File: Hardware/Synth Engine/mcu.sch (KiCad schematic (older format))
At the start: 32 parts, among them J10 USB_C_Receptacle, J3 SWD_programming, J7 Capsense_buttons, U6 CY8C4246AZI-L445, Y1 16MHz, Y2 32.768kHz

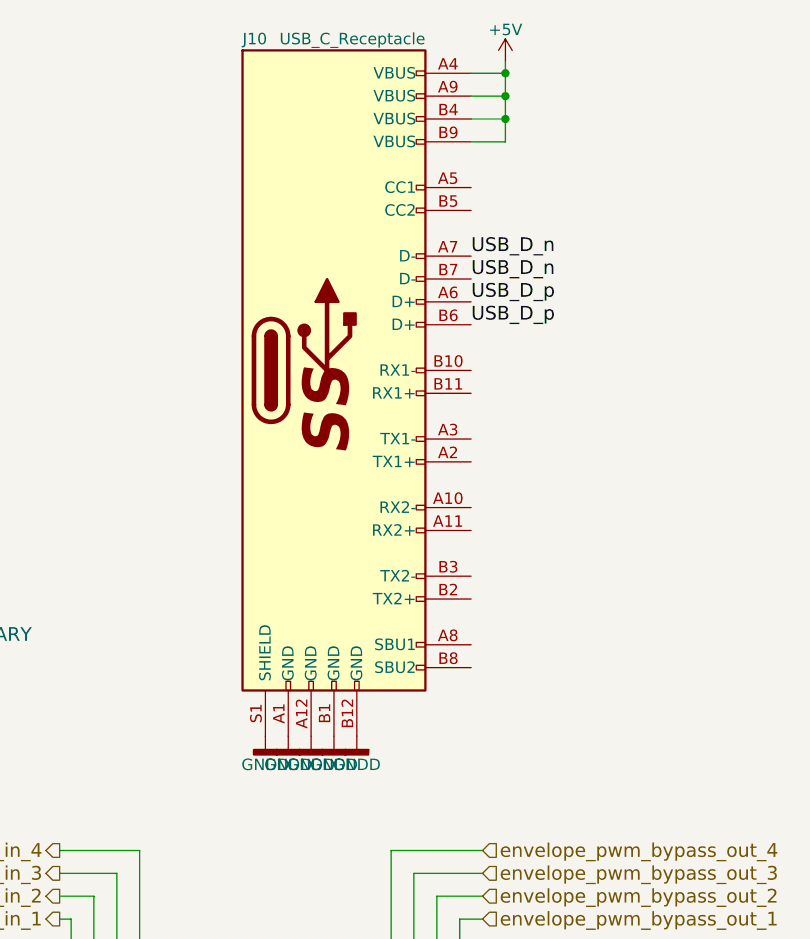
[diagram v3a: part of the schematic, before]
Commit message: redo second connector on main board
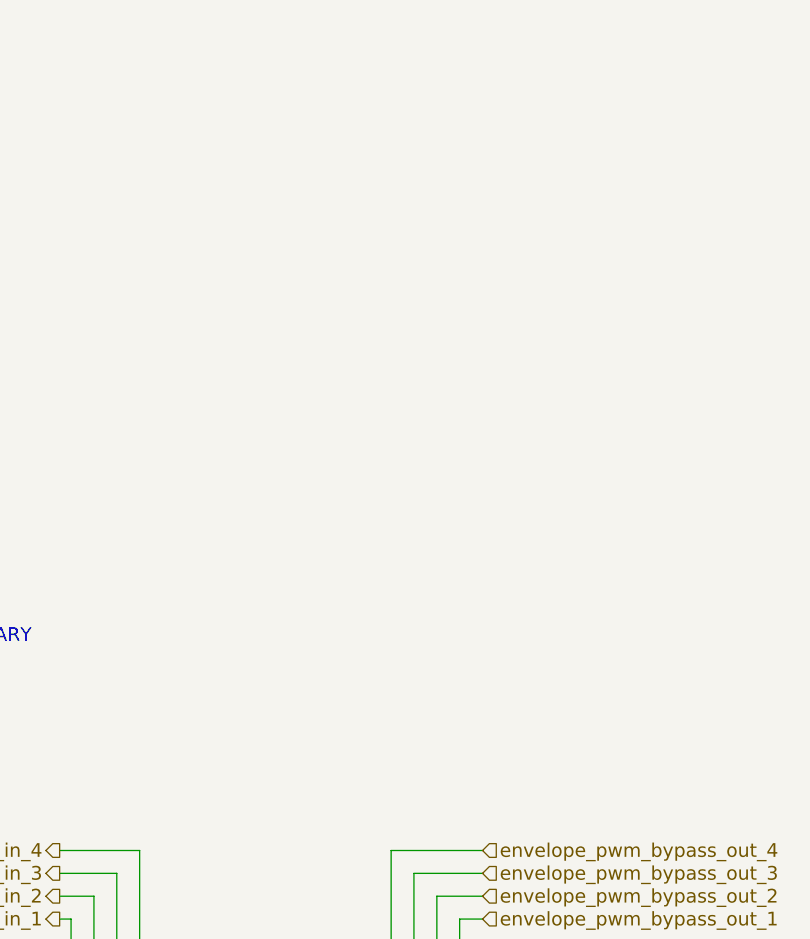
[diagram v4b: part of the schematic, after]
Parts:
- removed J10: USB_C_Receptacle, digikey-footprints:USB_Type_C_Female__12401610E4_2A, symbol USB_C_Receptacle
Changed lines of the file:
@@
 Text Notes 6350 3550 0    60   ~ 0
 Delay pins are TEMPORARY
-$Comp
-L USB_C_Receptacle J10
-U 1 1 5C748784
-P 8800 2350
-F 0 "J10" H 8400 3800 50  0000 L CNN
-F 1 "USB_C_Receptacle" H 9200 3800 50  0000 R CNN
-F 2 "digikey-footprints:USB_Type_C_Female__12401610E4_2A" H 8950 2350 50  0001 C CNN
-F 3 "" H 8950 2350 50  0001 C CNN
-	1    8800 2350
-	1    0    0    -1
-$EndComp
-$Comp
-L GNDD #PWR0106
-U 1 1 5C748857
-P 8900 3950
-F 0 "#PWR0106" H 8900 3700 50  0001 C CNN
-F 1 "GNDD" H 8900 3825 50  0000 C CNN
-F 2 "" H 8900 3950 50  0001 C CNN
-F 3 "" H 8900 3950 50  0001 C CNN
-	1    8900 3950
-	-1   0    0    -1
-$EndComp
-$Comp
-L GNDD #PWR0107
-U 1 1 5C74890A
-P 8800 3950
-F 0 "#PWR0107" H 8800 3700 50  0001 C CNN
-F 1 "GNDD" H 8800 3825 50  0000 C CNN
-F 2 "" H 8800 3950 50  0001 C CNN
-F 3 "" H 8800 3950 50  0001 C CNN
-	1    8800 3950
-	-1   0    0    -1
-$EndComp
-$Comp
-L GNDD #PWR0108
-U 1 1 5C748969
-P 8700 3950
-F 0 "#PWR0108" H 8700 3700 50  0001 C CNN
-F 1 "GNDD" H 8700 3825 50  0000 C CNN
-F 2 "" H 8700 3950 50  0001 C CNN
-F 3 "" H 8700 3950 50  0001 C CNN
-	1    8700 3950
-	-1   0    0    -1
-$EndComp
-$Comp
-L GNDD #PWR0109
-U 1 1 5C7489C8
-P 8600 3950
-F 0 "#PWR0109" H 8600 3700 50  0001 C CNN
-F 1 "GNDD" H 8600 3825 50  0000 C CNN
-F 2 "" H 8600 3950 50  0001 C CNN
-F 3 "" H 8600 3950 50  0001 C CNN
-	1    8600 3950
-	-1   0    0    -1
-$EndComp
-$Comp
-L GNDD #PWR0110
-U 1 1 5C748A27
-P 8500 3950
-F 0 "#PWR0110" H 8500 3700 50  0001 C CNN
-F 1 "GNDD" H 8500 3825 50  0000 C CNN
-F 2 "" H 8500 3950 50  0001 C CNN
-F 3 "" H 8500 3950 50  0001 C CNN
-	1    8500 3950
-	-1   0    0    -1
-$EndComp
-Text Label 9400 2150 0    60   ~ 0
-USB_D_p
-Text Label 9400 2050 0    60   ~ 0
-USB_D_p
-Text Label 9400 1950 0    60   ~ 0
-USB_D_n
-Text Label 9400 1850 0    60   ~ 0
-USB_D_n
 Text Label 2150 2850 2    60   ~ 0
 USB_D_p
@@
 USB_D_n
 $Comp
-L +5V #PWR0111
-U 1 1 5C74952F
-P 9550 1000
-F 0 "#PWR0111" H 9550 850 50  0001 C CNN
-F 1 "+5V" H 9550 1140 50  0000 C CNN
-F 2 "" H 9550 1000 50  0001 C CNN
-F 3 "" H 9550 1000 50  0001 C CNN
-	1    9550 1000
-	1    0    0    -1
-$EndComp
-$Comp
-L +5V #PWR0112
+L +5V #PWR0106
 U 1 1 5C7498B1
 P 2100 2600
-F 0 "#PWR0112" H 2100 2450 50  0001 C CNN
+F 0 "#PWR0106" H 2100 2450 50  0001 C CNN
 F 1 "+5V" H 2100 2740 50  0000 C CNN
 F 2 "" H 2100 2600 50  0001 C CNN
@@
 $EndComp
 $Comp
-L GNDD #PWR0113
+L GNDD #PWR0107
 U 1 1 5C74C9C5
 P 6050 2350
-F 0 "#PWR0113" H 6050 2100 50  0001 C CNN
+F 0 "#PWR0107" H 6050 2100 50  0001 C CNN
 F 1 "GNDD" H 6050 2225 50  0000 C CNN
 F 2 "" H 6050 2350 50  0001 C CNN
@@
 $EndComp
 $Comp
-L GNDD #PWR0114
+L GNDD #PWR0108
 U 1 1 5C74C9CB
 P 6550 2350
-F 0 "#PWR0114" H 6550 2100 50  0001 C CNN
+F 0 "#PWR0108" H 6550 2100 50  0001 C CNN
 F 1 "GNDD" H 6550 2225 50  0000 C CNN
 F 2 "" H 6550 2350 50  0001 C CNN
@@
 	5950 4500 5950 4450
 Wire Wire Line
-	9550 1000 9550 1350
-Wire Wire Line
-	9550 1350 9400 1350
-Wire Wire Line
-	9400 1250 9550 1250
-Connection ~ 9550 1250
-Wire Wire Line
-	9400 1150 9550 1150
-Connection ~ 9550 1150
-Wire Wire Line
-	9400 1050 9550 1050
-Connection ~ 9550 1050
-Wire Wire Line
 	2100 2600 2100 2650

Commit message: new release candidate. Passes DRC.
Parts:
- added J10: USB, Connectors_Molex:Molex_KK-6410-04_04x2.54mm_Straight, symbol Conn_01x04
- J7: footprint Pin_Headers:Pin_Header_Straight_1x04_Pitch2.54mm -> Connectors_Molex:Molex_KK-6410-04_04x2.54mm_Straight
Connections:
- net +5V: now also J10.1 (Pin_1)
- net GNDD: now also J10.4 (Pin_4)
- net USB_D_n: now also J10.2 (Pin_2)
- net USB_D_p: now also J10.3 (Pin_3)
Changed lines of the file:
@@
 F 0 "J7" H 6150 4550 50  0000 C CNN
 F 1 "Capsense_buttons" H 6550 4300 50  0000 C CNN
-F 2 "Pin_Headers:Pin_Header_Straight_1x04_Pitch2.54mm" H 6150 4350 50  0001 C CNN
+F 2 "Connectors_Molex:Molex_KK-6410-04_04x2.54mm_Straight" H 6150 4350 50  0001 C CNN
 F 3 "" H 6150 4350 50  0001 C CNN
 	1    6150 4350
@@
 Text HLabel 4950 1400 2    60   Input ~ 0
 osc4_hold
+$Comp
+L Conn_01x04 J10
+U 1 1 5C75AB8E
+P 8850 2450
+F 0 "J10" H 8850 2650 50  0000 C CNN
+F 1 "USB" H 9000 2400 50  0000 C CNN
+F 2 "Connectors_Molex:Molex_KK-6410-04_04x2.54mm_Straight" H 8850 2450 50  0001 C CNN
+F 3 "" H 8850 2450 50  0001 C CNN
+	1    8850 2450
+	1    0    0    -1
+$EndComp
+Text Label 8650 2550 2    60   ~ 0
+USB_D_p
+Text Label 8650 2450 2    60   ~ 0
+USB_D_n
+$Comp
+L GNDD #PWR0109
+U 1 1 5C75B32A
+P 8650 2650
+F 0 "#PWR0109" H 8650 2400 50  0001 C CNN
+F 1 "GNDD" H 8650 2525 50  0000 C CNN
+F 2 "" H 8650 2650 50  0001 C CNN
+F 3 "" H 8650 2650 50  0001 C CNN
+	1    8650 2650
+	1    0    0    -1
+$EndComp
+$Comp
+L +5V #PWR0110
+U 1 1 5C75B515
+P 8650 2350
+F 0 "#PWR0110" H 8650 2200 50  0001 C CNN
+F 1 "+5V" H 8650 2490 50  0000 C CNN
+F 2 "" H 8650 2350 50  0001 C CNN
+F 3 "" H 8650 2350 50  0001 C CNN
+	1    8650 2350
+	1    0    0    -1
+$EndComp
 $EndSCHEMATC

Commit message: add MIDI
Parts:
- added D3: D, digikey-footprints:SOT-23-3, symbol D
- added J11: MIDI IN, Connectors_Molex:Molex_KK-6410-02_02x2.54mm_Straight, symbol Conn_01x02
- added J12: MIDI OUT, Connectors_Molex:Molex_KK-6410-02_02x2.54mm_Straight, symbol Conn_01x02
- added Q9: 2N3904, digikey-footprints:SOT-23-3, symbol 2N3904
- added R100: 10k, digikey-footprints:0805, symbol R
- added R101, R102, R98: 220, digikey-footprints:0805, symbol R
- added R99: 280, digikey-footprints:0805, symbol R
- added U9: 4N28, digikey-footprints:DIP-8_W7.62mm, symbol 4N28
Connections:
- net +5V: now also R101.2, R99.2, U9.6
- net GNDD: now also Q9.1 (E), U9.4
- net MIDI_OUT: now reaches U6.33 (P4.6)
- net MIDI_OUT: now also R100.2
- net MIDI_IN: now reaches U6.40 (P0.1)
- net MIDI_IN: now also R99.1, U9.5
- new net: D3.1 (K), J11.1 (Pin_1), U9.1
- new net: J11.2 (Pin_2), R98.2
- new net: D3.2 (A), R98.1, U9.2
- new net: J12.1 (Pin_1), R101.1
- new net: J12.2 (Pin_2), R102.1
- new net: Q9.3 (C), R102.2
- new net: Q9.2 (B), R100.1
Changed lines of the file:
@@
 	1    0    0    -1
 $EndComp
+$Comp
+L Conn_01x02 J11
+U 1 1 5C76FED3
+P 2350 6950
+F 0 "J11" H 2350 7050 50  0000 C CNN
+F 1 "MIDI IN" H 2350 6750 50  0000 C CNN
+F 2 "Connectors_Molex:Molex_KK-6410-02_02x2.54mm_Straight" H 2350 6950 50  0001 C CNN
+F 3 "" H 2350 6950 50  0001 C CNN
+	1    2350 6950
+	-1   0    0    -1
+$EndComp
+$Comp
+L D D3
+U 1 1 5C76FEDB
+P 3050 7100
+F 0 "D3" H 3050 7200 50  0000 C CNN
+F 1 "D" H 3050 7000 50  0000 C CNN
+F 2 "digikey-footprints:SOT-23-3" H 3050 7100 50  0001 C CNN
+F 3 "" H 3050 7100 50  0001 C CNN
+	1    3050 7100
+	0    1    1    0
+$EndComp
+Wire Wire Line
+	2900 7250 3150 7250
+Wire Wire Line
+	3150 7250 3150 7150
+Wire Wire Line
+	2550 7050 2550 7250
+Connection ~ 3050 7250
+$Comp
+L R R98
+U 1 1 5C76FEE6
+P 2750 7250
+F 0 "R98" V 2830 7250 50  0000 C CNN
+F 1 "220" V 2750 7250 50  0000 C CNN
+F 2 "digikey-footprints:0805" V 2680 7250 50  0001 C CNN
+F 3 "" H 2750 7250 50  0001 C CNN
+	1    2750 7250
+	0    1    1    0
+$EndComp
+Wire Wire Line
+	2550 7250 2600 7250
+$Comp
+L 4N28 U9
+U 1 1 5C76FEEE
+P 3700 7050
+F 0 "U9" H 3500 7250 50  0000 L CNN
+F 1 "4N28" H 3700 7250 50  0000 L CNN
+F 2 "digikey-footprints:DIP-8_W7.62mm" H 3500 6850 50  0001 L CIN
+F 3 "" H 3700 7050 50  0001 L CNN
+	1    3700 7050
+	1    0    0    -1
+$EndComp
+Wire Wire Line
+	3150 7150 3400 7150
+$Comp
+L +5V #PWR0111
+U 1 1 5C76FEF6
+P 4050 6650
+F 0 "#PWR0111" H 4050 6500 50  0001 C CNN
+F 1 "+5V" H 4050 6790 50  0000 C CNN
+F 2 "" H 4050 6650 50  0001 C CNN
+F 3 "" H 4050 6650 50  0001 C CNN
+	1    4050 6650
+	1    0    0    -1
+$EndComp
+Wire Wire Line
+	4050 6650 4200 6650
+Wire Wire Line
+	4050 6650 4050 6950
+Wire Wire Line
+	4050 6950 4000 6950
+$Comp
+L GNDD #PWR0112
+U 1 1 5C76FEFE
+P 4050 7250
+F 0 "#PWR0112" H 4050 7000 50  0001 C CNN
+F 1 "GNDD" H 4050 7125 50  0000 C CNN
+F 2 "" H 4050 7250 50  0001 C CNN
+F 3 "" H 4050 7250 50  0001 C CNN
+	1    4050 7250
+	1    0    0    -1
+$EndComp
+Wire Wire Line
+	4050 7250 4050 7150
+Wire Wire Line
+	4050 7150 4000 7150
+Text Label 5150 1300 0    60   ~ 0
+MIDI_IN
+Wire Wire Line
+	5150 1300 4950 1300
+Text Label 4350 7050 0    60   ~ 0
+MIDI_IN
+Wire Wire Line
+	4000 7050 4350 7050
+Text Label 5100 4800 0    60   ~ 0
+MIDI_OUT
+$Comp
+L R R99
+U 1 1 5C773277
+P 4200 6850
+F 0 "R99" V 4280 6850 50  0000 C CNN
+F 1 "280" V 4200 6850 50  0000 C CNN
+F 2 "digikey-footprints:0805" V 4130 6850 50  0001 C CNN
+F 3 "" H 4200 6850 50  0001 C CNN
+	1    4200 6850
+	-1   0    0    1
+$EndComp
+Wire Wire Line
+	4200 6650 4200 6700
+Connection ~ 4050 6650
+Wire Wire Line
+	4200 7000 4200 7050
+Connection ~ 4200 7050
+$Comp
+L Conn_01x02 J12
+U 1 1 5C773A8A
+P 6700 6900
+F 0 "J12" H 6700 7000 50  0000 C CNN
+F 1 "MIDI OUT" H 6700 6700 50  0000 C CNN
+F 2 "Connectors_Molex:Molex_KK-6410-02_02x2.54mm_Straight" H 6700 6900 50  0001 C CNN
+F 3 "" H 6700 6900 50  0001 C CNN
+	1    6700 6900
+	1    0    0    -1
+$EndComp
+$Comp
+L R R101
+U 1 1 5C773E85
+P 6350 6900
+F 0 "R101" V 6430 6900 50  0000 C CNN
+F 1 "220" V 6350 6900 50  0000 C CNN
+F 2 "digikey-footprints:0805" V 6280 6900 50  0001 C CNN
+F 3 "" H 6350 6900 50  0001 C CNN
+	1    6350 6900
+	0    1    1    0
+$EndComp
+$Comp
+L R R102
+U 1 1 5C773F46
+P 6350 7000
+F 0 "R102" V 6430 7000 50  0000 C CNN
+F 1 "220" V 6350 7000 50  0000 C CNN
+F 2 "digikey-footprints:0805" V 6280 7000 50  0001 C CNN
+F 3 "" H 6350 7000 50  0001 C CNN
+	1    6350 7000
+	0    1    1    0
+$EndComp
+Text Label 5400 7300 2    60   ~ 0
+MIDI_OUT
+$Comp
+L +5V #PWR0113
+U 1 1 5C774E5B
+P 6150 6800
+F 0 "#PWR0113" H 6150 6650 50  0001 C CNN
+F 1 "+5V" H 6150 6940 50  0000 C CNN
+F 2 "" H 6150 6800 50  0001 C CNN
+F 3 "" H 6150 6800 50  0001 C CNN
+	1    6150 6800
+	1    0    0    -1
+$EndComp
+Wire Wire Line
+	6150 6800 6150 6900
+Wire Wire Line
+	6150 6900 6200 6900
+$Comp
+L 2N3904 Q9
+U 1 1 5C77538C
+P 5900 7300
+F 0 "Q9" H 6100 7375 50  0000 L CNN
+F 1 "2N3904" H 6100 7300 50  0000 L CNN
+F 2 "digikey-footprints:SOT-23-3" H 6100 7225 50  0001 L CIN
+F 3 "" H 5900 7300 50  0001 L CNN
+	1    5900 7300
+	1    0    0    -1
+$EndComp
+$Comp
+L R R100
+U 1 1 5C775480
+P 5550 7300
+F 0 "R100" V 5630 7300 50  0000 C CNN
+F 1 "10k" V 5550 7300 50  0000 C CNN
+F 2 "digikey-footprints:0805" V 5480 7300 50  0001 C CNN
+F 3 "" H 5550 7300 50  0001 C CNN
+	1    5550 7300
+	0    1    1    0
+$EndComp
+Wire Wire Line
+	6000 7100 6000 7000
+$Comp
+L GNDD #PWR0114
+U 1 1 5C775709
+P 6000 7500
+F 0 "#PWR0114" H 6000 7250 50  0001 C CNN
+F 1 "GNDD" H 6000 7375 50  0000 C CNN
+F 2 "" H 6000 7500 50  0001 C CNN
+F 3 "" H 6000 7500 50  0001 C CNN
+	1    6000 7500
+	1    0    0    -1
+$EndComp
+Wire Wire Line
+	6000 7000 6200 7000
+Wire Wire Line
+	2550 6950 3400 6950
+Connection ~ 3050 6950
+Wire Wire Line
+	5100 4800 4950 4800
 $EndSCHEMATC

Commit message: arrange reference designators on main board
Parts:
- J10, J7: footprint Connectors_Molex:Molex_KK-6410-04_04x2.54mm_Straight -> Pin_Headers:Pin_Header_Straight_1x04_Pitch2.00mm
- J11, J12: footprint Connectors_Molex:Molex_KK-6410-02_02x2.54mm_Straight -> Pin_Headers:Pin_Header_Straight_1x02_Pitch2.00mm
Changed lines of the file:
@@
 F 0 "J7" H 6150 4550 50  0000 C CNN
 F 1 "Capsense_buttons" H 6550 4300 50  0000 C CNN
-F 2 "Connectors_Molex:Molex_KK-6410-04_04x2.54mm_Straight" H 6150 4350 50  0001 C CNN
+F 2 "Pin_Headers:Pin_Header_Straight_1x04_Pitch2.00mm" H 6150 4350 50  0001 C CNN
 F 3 "" H 6150 4350 50  0001 C CNN
 	1    6150 4350
@@
 F 0 "J10" H 8850 2650 50  0000 C CNN
 F 1 "USB" H 9000 2400 50  0000 C CNN
-F 2 "Connectors_Molex:Molex_KK-6410-04_04x2.54mm_Straight" H 8850 2450 50  0001 C CNN
+F 2 "Pin_Headers:Pin_Header_Straight_1x04_Pitch2.00mm" H 8850 2450 50  0001 C CNN
 F 3 "" H 8850 2450 50  0001 C CNN
 	1    8850 2450
@@
 F 0 "J11" H 2350 7050 50  0000 C CNN
 F 1 "MIDI IN" H 2350 6750 50  0000 C CNN
-F 2 "Connectors_Molex:Molex_KK-6410-02_02x2.54mm_Straight" H 2350 6950 50  0001 C CNN
+F 2 "Pin_Headers:Pin_Header_Straight_1x02_Pitch2.00mm" H 2350 6950 50  0001 C CNN
 F 3 "" H 2350 6950 50  0001 C CNN
 	1    2350 6950
@@
 F 0 "J12" H 6700 7000 50  0000 C CNN
 F 1 "MIDI OUT" H 6700 6700 50  0000 C CNN
-F 2 "Connectors_Molex:Molex_KK-6410-02_02x2.54mm_Straight" H 6700 6900 50  0001 C CNN
+F 2 "Pin_Headers:Pin_Header_Straight_1x02_Pitch2.00mm" H 6700 6900 50  0001 C CNN
 F 3 "" H 6700 6900 50  0001 C CNN
 	1    6700 6900

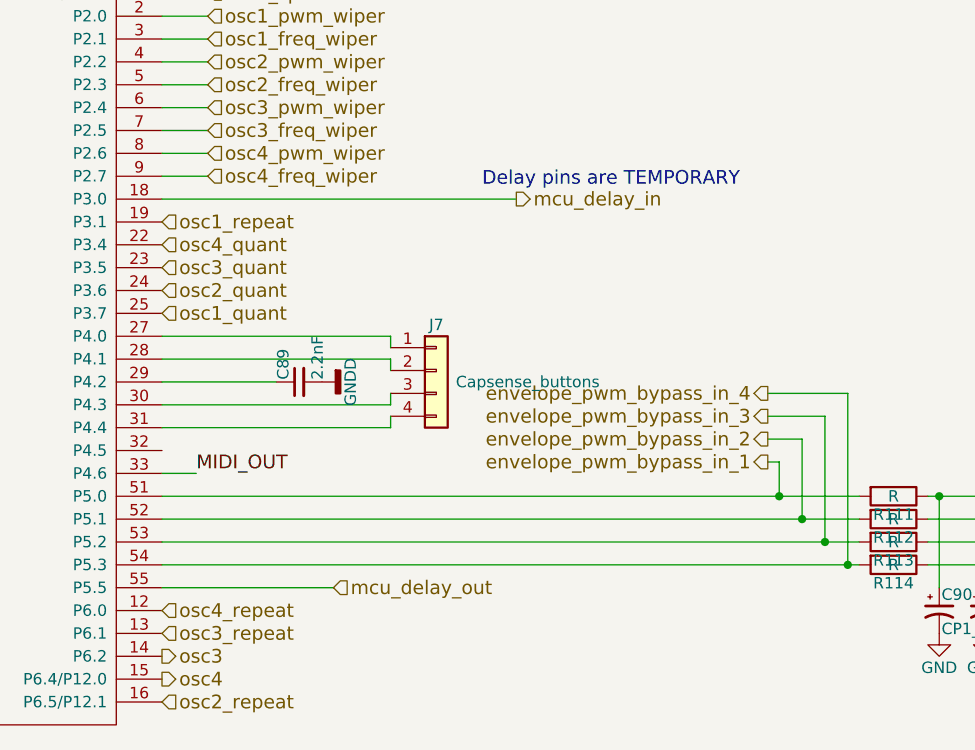
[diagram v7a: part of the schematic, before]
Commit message: add missing RC feedback network for MCU delay. Probably won't end up using this, but it's there if I need it.
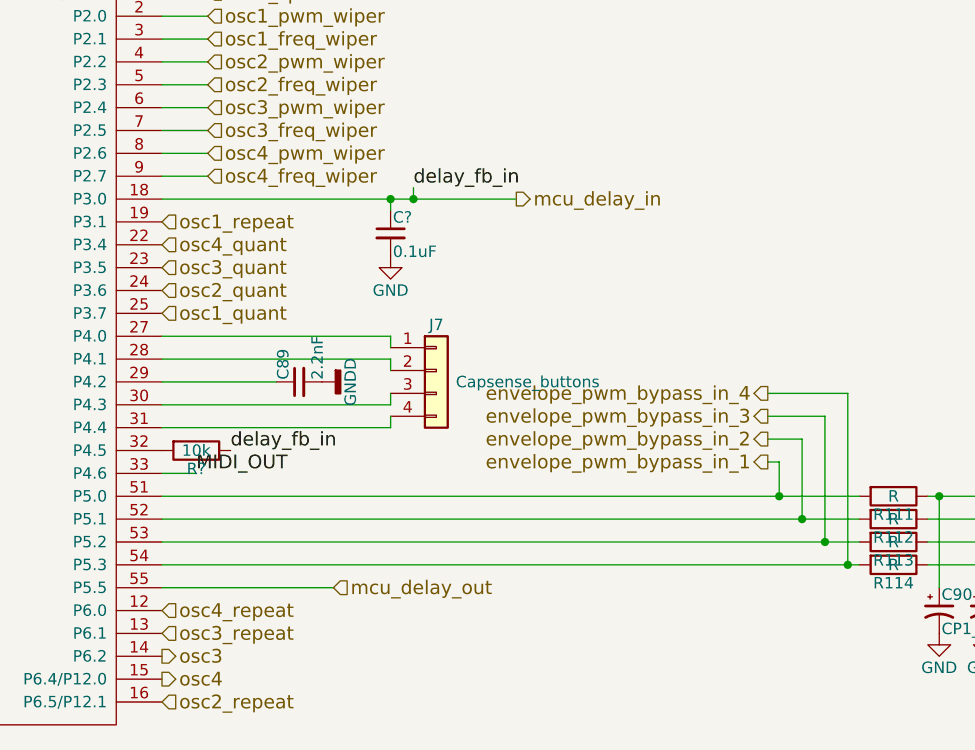
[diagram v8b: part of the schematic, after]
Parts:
- added C?: 0.1uF, digikey-footprints:0805, symbol C_Small
- added R?: 10k, digikey-footprints:0805, symbol R
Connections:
- net GND: now also C?.2
- net mcu_delay_in: now also C?.1, R?.1
- net at U6.32 (P4.5): now also R?.2
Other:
- note removed: "Delay pins are TEMPORARY"
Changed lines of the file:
@@
 Text HLabel 4950 3800 2    60   Input ~ 0
 osc4_quant
-Text Notes 6350 3550 0    60   ~ 0
-Delay pins are TEMPORARY
 Text Label 2150 2850 2    60   ~ 0
 USB_D_p
@@
 Wire Wire Line
 	5600 2300 4950 2300
-Wire Wire Line
-	6500 3600 4950 3600
-Wire Wire Line
-	5700 5300 4950 5300
 Wire Wire Line
 	5950 4250 5950 4200
@@
 Wire Wire Line
 	5100 4800 4950 4800
+$Comp
+L R R?
+U 1 1 5C77CA4F
+P 5100 4700
+F 0 "R?" V 5180 4700 50  0000 C CNN
+F 1 "10k" V 5100 4700 50  0000 C CNN
+F 2 "digikey-footprints:0805" V 5030 4700 50  0001 C CNN
+F 3 "" H 5100 4700 50  0001 C CNN
+	1    5100 4700
+	0    1    1    0
+$EndComp
+Wire Wire Line
+	4950 3600 6500 3600
+$Comp
+L C_Small C?
+U 1 1 5C77D660
+P 5950 3750
+F 0 "C?" H 5960 3820 50  0000 L CNN
+F 1 "0.1uF" H 5960 3670 50  0000 L CNN
+F 2 "digikey-footprints:0805" H 5950 3750 50  0001 C CNN
+F 3 "" H 5950 3750 50  0001 C CNN
+	1    5950 3750
+	1    0    0    -1
+$EndComp
+Wire Wire Line
+	5950 3650 5950 3600
+Connection ~ 5950 3600
+$Comp
+L GND #PWR?
+U 1 1 5C77D97F
+P 5950 3850
+F 0 "#PWR?" H 5950 3600 50  0001 C CNN
+F 1 "GND" H 5950 3700 50  0000 C CNN
+F 2 "" H 5950 3850 50  0001 C CNN
+F 3 "" H 5950 3850 50  0001 C CNN
+	1    5950 3850
+	1    0    0    -1
+$EndComp
+Wire Wire Line
+	4950 5300 5700 5300
+Text Label 6050 3550 0    60   ~ 0
+delay_fb_in
+Text Label 5250 4700 0    60   ~ 0
+delay_fb_in
+Wire Wire Line
+	6050 3550 6050 3600
+Connection ~ 6050 3600
 $EndSCHEMATC
